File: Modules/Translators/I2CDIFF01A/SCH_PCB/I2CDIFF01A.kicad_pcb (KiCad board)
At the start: 2 copper layers, 40.1 x 50.3 mm, 55 parts, among them J1 JUMP_4X2, J10 JUMP_3X2, J11 JUMP2_2x1, J12 CONN_3, J13 JUMP_3X2, J14 JUMP2_2x1, J15 CONN_3, J16 EN, J17 JUMP2_2x1, J19 JUMP_2x1, J2 RJ45_RJHSE-5384, J20 JUMP_2x1, J21 JUMP_2x1, J22 JUMP_2x1, J23 JUMP_2x1, J3 JUMP_2x1, J4 JUMP_2x1, J5 JUMP_2x1, J6 JUMP_2x1, J7 JUMP_2x1, J8 JUMP_2x1, J9 JUMP_2x1, M1 HOLE, M2 HOLE, M3 HOLE, M4 HOLE, U1 LM1117 5V, U2 LM1117 3V3, U3 PCA9616

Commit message: vylepseni layoutu.
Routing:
- net /SCL-: track 41.5 -> 39.9 mm
- net /SCL+: track 40.7 -> 39.2 mm
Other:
- rule via_min_size: 0.89 -> 0.7

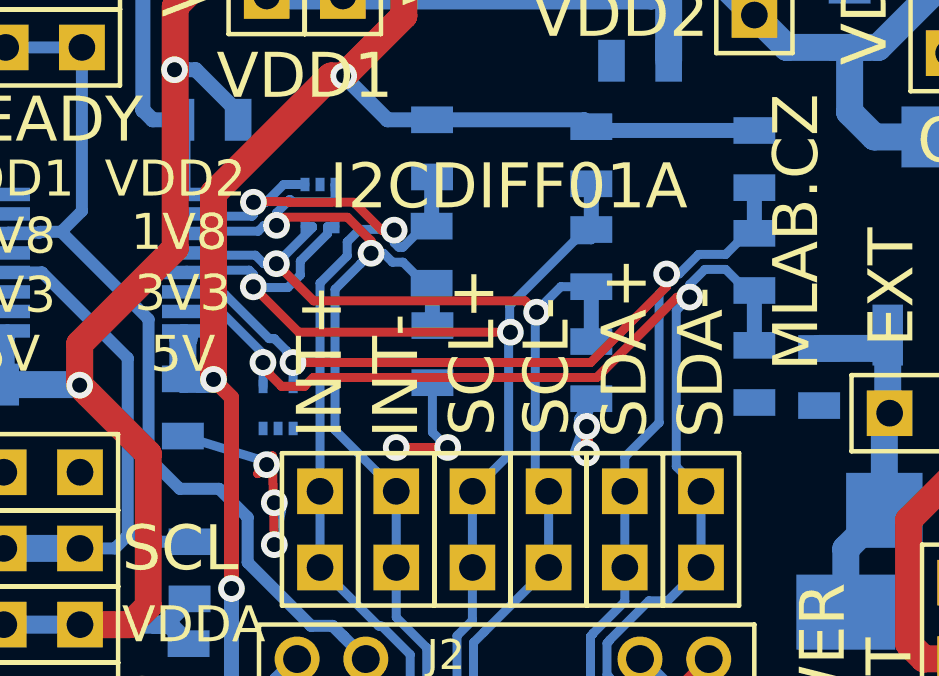
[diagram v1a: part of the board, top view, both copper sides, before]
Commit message: 
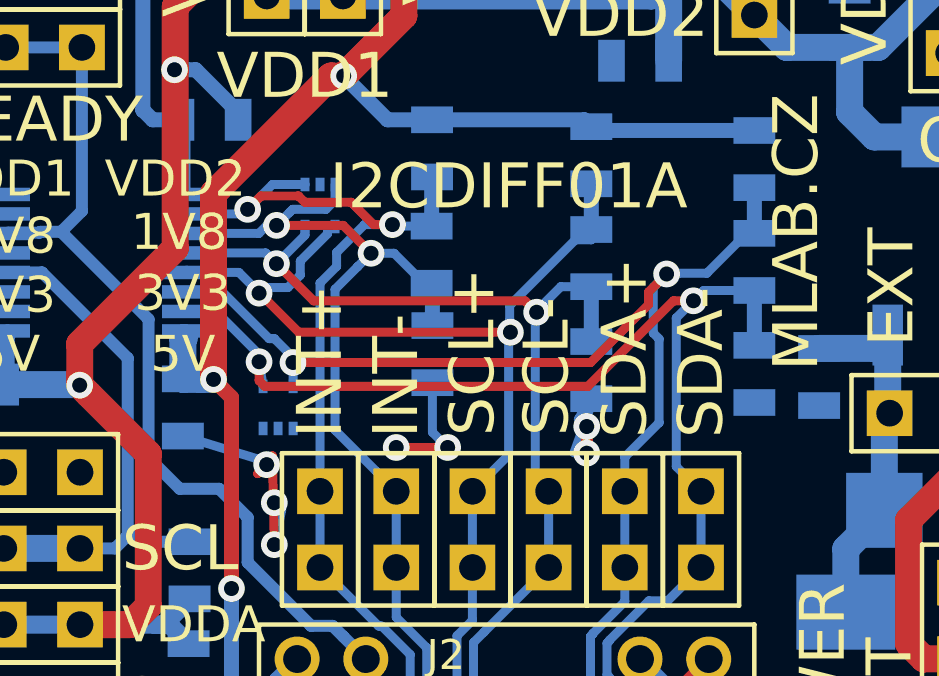
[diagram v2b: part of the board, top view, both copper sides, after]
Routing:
- net /INT-: track 37.3 -> 36.6 mm
- net /SDA-: track 46.3 -> 45.6 mm

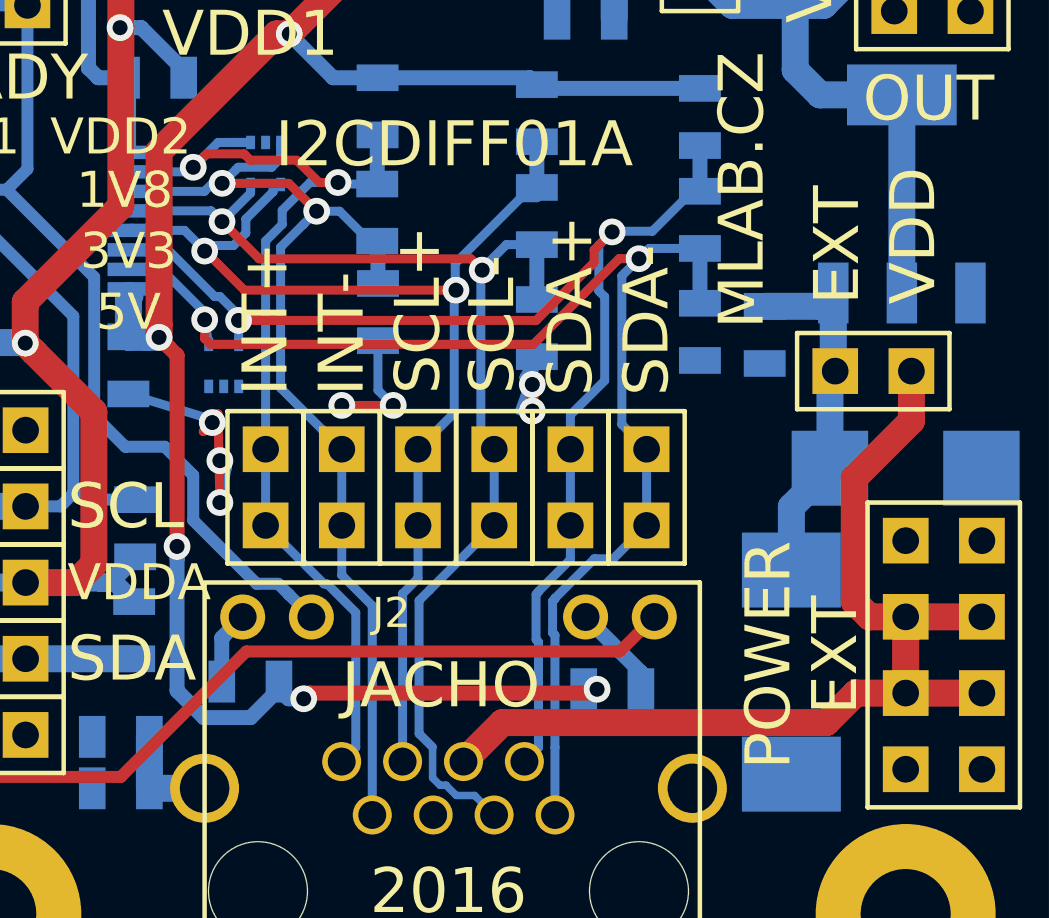
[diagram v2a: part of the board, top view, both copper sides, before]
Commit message: vylepseni layoutu differencnich cest.
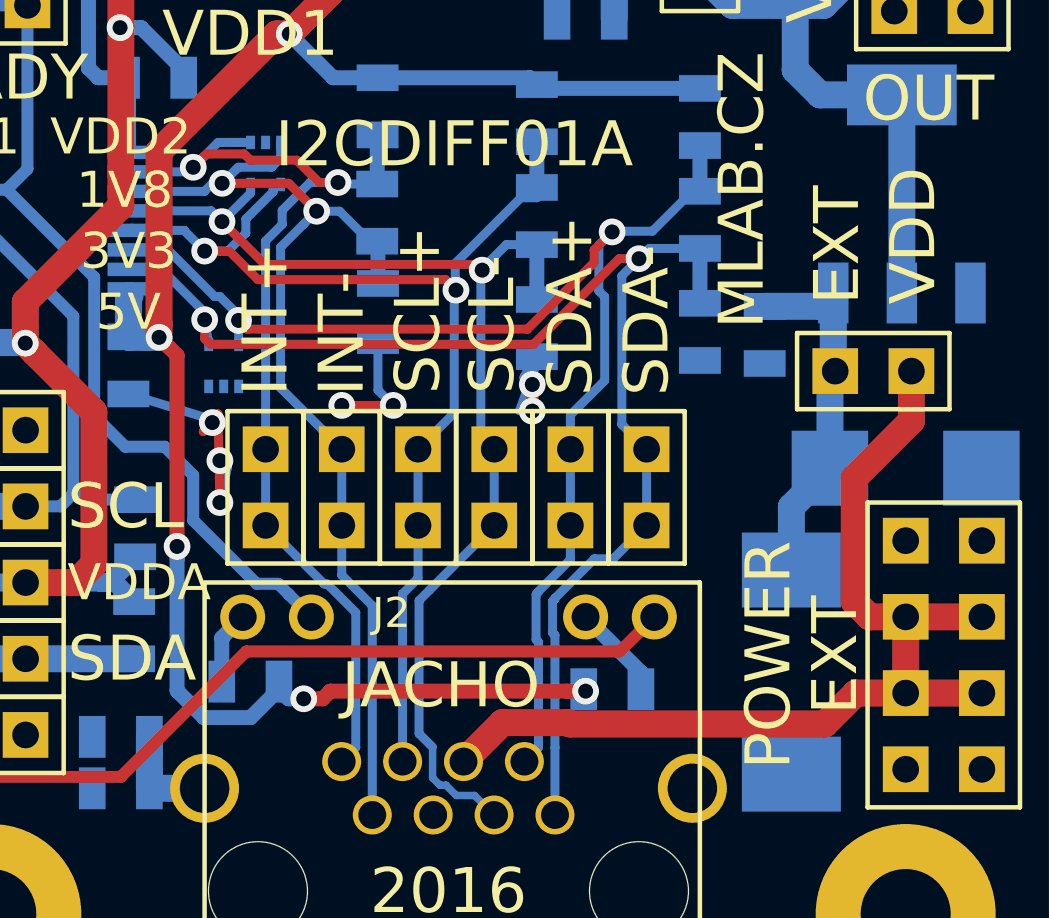
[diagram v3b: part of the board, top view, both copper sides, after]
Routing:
- net /VddB: track 65.4 -> 64.6 mm
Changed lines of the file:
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@@
-(kicad_pcb (version 4) (host pcbnew 4.0.1-stable)
+(kicad_pcb (version 4) (host pcbnew 0.201602161416+6560~42~ubuntu15.10.1-product)
   (general
     (links 132)
@@
     (thickness 1.6)
     (drawings 44)
-    (tracks 413)
+    (tracks 420)
     (zones 0)
     (modules 55)
@@
     (visible_elements 7FFFFF7F)
     (pcbplotparams
-      (layerselection 0x010e0_80000001)
+      (layerselection 0x010e0_ffffffff)
       (usegerberextensions false)
       (excludeedgelayer true)
@@
       (hpglpenspeed 20)
       (hpglpendiameter 15)
-      (hpglpenoverlay 2)
       (psnegative false)
       (psa4output false)
@@
   (gr_line (start 40.386 -0.254) (end 40.386 -50.546) (angle 90) (layer Edge.Cuts) (width 0.1))
   (gr_line (start 0.254 -0.254) (end 40.386 -0.254) (angle 90) (layer Edge.Cuts) (width 0.1))
+  (segment (start 24.318897 -11.462001) (end 24.366399 -11.414499) (width 0.9) (layer F.Cu) (net 1))
+  (segment (start 20.82 -10.162) (end 22.120001 -11.462001) (width 0.9) (layer F.Cu) (net 1))
+  (segment (start 22.120001 -11.462001) (end 24.318897 -11.462001) (width 0.9) (layer F.Cu) (net 1))
+  (segment (start 24.366399 -11.414499) (end 32.866499 -11.414499) (width 0.9) (layer F.Cu) (net 1))
+  (segment (start 32.866499 -11.414499) (end 33.898 -12.446) (width 0.9) (layer F.Cu) (net 1))
   (segment (start 33.898 -12.446) (end 35.56 -12.446) (width 0.9) (layer F.Cu) (net 1))
-  (segment (start 32.914001 -11.462001) (end 33.898 -12.446) (width 0.9) (layer F.Cu) (net 1))
-  (segment (start 22.120001 -11.462001) (end 32.914001 -11.462001) (width 0.9) (layer F.Cu) (net 1))
-  (segment (start 20.82 -10.162) (end 22.120001 -11.462001) (width 0.9) (layer F.Cu) (net 1))
   (segment (start 35.56 -12.446) (end 38.1 -12.446) (width 0.9) (layer F.Cu) (net 1))
   (segment (start 35.56 -12.446) (end 35.56 -14.986) (width 0.9) (layer F.Cu) (net 1))
@@
   (segment (start 23.368 -48.133) (end 23.368 -45.593) (width 0.9) (layer B.Cu) (net 4))
   (segment (start 12.446 -42.164) (end 14.986 -42.164) (width 0.9) (layer B.Cu) (net 4))
-  (segment (start 25.273 -12.573) (end 25.146 -12.446) (width 0.5) (layer F.Cu) (net 5))
-  (segment (start 15.6845 -12.446) (end 15.494 -12.2555) (width 0.5) (layer F.Cu) (net 5))
-  (segment (start 25.146 -12.446) (end 15.6845 -12.446) (width 0.5) (layer F.Cu) (net 5))
+  (segment (start 24.262675 -12.5095) (end 24.892 -12.5095) (width 0.5) (layer F.Cu) (net 5))
+  (segment (start 16.377325 -12.5095) (end 24.262675 -12.5095) (width 0.5) (layer F.Cu) (net 5))
+  (via (at 24.892 -12.5095) (size 0.89) (drill 0.5) (layers F.Cu B.Cu) (net 5))
+  (segment (start 16.123325 -12.2555) (end 16.377325 -12.5095) (width 0.5) (layer F.Cu) (net 5))
+  (segment (start 15.494 -12.2555) (end 16.123325 -12.2555) (width 0.5) (layer F.Cu) (net 5))
+  (segment (start 24.8285 -12.573) (end 24.892 -12.5095) (width 0.5) (layer B.Cu) (net 5))
   (segment (start 14.986 -12.2555) (end 15.069736 -12.2555) (width 0.5) (layer B.Cu) (net 5))
   (segment (start 14.6685 -12.573) (end 14.986 -12.2555) (width 0.5) (layer B.Cu) (net 5))
@@
   (segment (start 9.7064 -25.919) (end 9.7064 -24.3749) (width 0.25) (layer B.Cu) (net 5))
   (segment (start 9.7064 -24.3749) (end 9.652 -24.3205) (width 0.25) (layer B.Cu) (net 5))
-  (segment (start 24.8285 -12.573) (end 25.273 -12.573) (width 0.5) (layer B.Cu) (net 5))
-  (via (at 25.273 -12.573) (size 0.89) (drill 0.5) (layers F.Cu B.Cu) (net 5))
   (segment (start 28.702 -32.6009) (end 23.3934 -32.6009) (width 0.5) (layer B.Cu) (net 5))
   (segment (start 23.3934 -32.6009) (end 23.2664 -32.7279) (width 0.5) (layer B.Cu) (net 5))
@@
   (segment (start 17.78 -8.382) (end 17.78 -15.357806) (width 0.3) (layer B.Cu) (net 12))
   (segment (start 17.9578 -27.4955) (end 17.9451 -27.5082) (width 0.5) (layer B.Cu) (net 12))
-  (segment (start 21.443851 -26.542524) (end 21.066375 -26.92) (width 0.3) (layer F.Cu) (net 13))
-  (segment (start 21.066375 -26.92) (end 14.011074 -26.92) (width 0.3) (layer F.Cu) (net 13))
-  (segment (start 14.011074 -26.92) (end 12.770702 -28.160372) (width 0.3) (layer F.Cu) (net 13))
+  (segment (start 21.443851 -26.542524) (end 21.252875 -26.7335) (width 0.3) (layer F.Cu) (net 13))
+  (segment (start 21.252875 -26.7335) (end 14.197574 -26.7335) (width 0.3) (layer F.Cu) (net 13))
+  (segment (start 14.197574 -26.7335) (end 12.770702 -28.160372) (width 0.3) (layer F.Cu) (net 13))
   (segment (start 9.7064 -28.519) (end 12.412074 -28.519) (width 0.3) (layer B.Cu) (net 13))
   (segment (start 12.412074 -28.519) (end 12.770702 -28.160372) (width 0.3) (layer B.Cu) (net 13))
@@
   (segment (start 19.339999 -15.529999) (end 19.692908 -15.882908) (width 0.3) (layer B.Cu) (net 13))
   (segment (start 19.692908 -15.882908) (end 21.844 -18.034) (width 0.3) (layer B.Cu) (net 13))
+  (segment (start 11.520582 -27.869) (end 11.520582 -27.849418) (width 0.3) (layer B.Cu) (net 14))
+  (segment (start 11.520582 -27.849418) (end 12.192 -27.178) (width 0.3) (layer B.Cu) (net 14))
+  (segment (start 14.72438 -29.39796) (end 14.474 -29.39796) (width 0.3) (layer B.Cu) (net 14))
+  (segment (start 14.474 -29.39796) (end 14.474 -29.156564) (width 0.3) (layer B.Cu) (net 14))
+  (segment (start 14.474 -29.156564) (end 13.565703 -28.248267) (width 0.3) (layer B.Cu) (net 14))
+  (segment (start 13.565703 -28.248267) (end 13.565703 -27.778771) (width 0.3) (layer B.Cu) (net 14))
+  (segment (start 13.565703 -27.778771) (end 12.964932 -27.178) (width 0.3) (layer B.Cu) (net 14))
+  (segment (start 12.964932 -27.178) (end 12.192 -27.178) (width 0.3) (layer B.Cu) (net 14))
+  (via (at 12.192 -27.178) (size 0.89) (drill 0.5) (layers F.Cu B.Cu) (net 14))
+  (segment (start 20.569627 -25.875237) (end 20.219364 -26.2255) (width 0.3) (layer F.Cu) (net 14))
+  (segment (start 12.821325 -27.178) (end 12.192 -27.178) (width 0.3) (layer F.Cu) (net 14))
+  (segment (start 20.219364 -26.2255) (end 13.97 -26.2255) (width 0.3) (layer F.Cu) (net 14))
+  (segment (start 13.97 -26.2255) (end 13.023175 -27.172325) (width 0.3) (layer F.Cu) (net 14))
+  (segment (start 13.023175 -27.172325) (end 12.827 -27.172325) (width 0.3) (layer F.Cu) (net 14))
+  (segment (start 12.827 -27.172325) (end 12.821325 -27.178) (width 0.3) (layer F.Cu) (net 14))
   (segment (start 9.7064 -27.869) (end 11.520582 -27.869) (width 0.3) (layer B.Cu) (net 14))
-  (segment (start 11.520582 -27.869) (end 11.999956 -27.389626) (width 0.3) (layer B.Cu) (net 14))
-  (segment (start 20.569627 -25.875237) (end 13.514345 -25.875237) (width 0.3) (layer F.Cu) (net 14))
-  (segment (start 13.514345 -25.875237) (end 11.999956 -27.389626) (width 0.3) (layer F.Cu) (net 14))
   (segment (start 19.304 -20.574) (end 20.5105 -21.7805) (width 0.3) (layer B.Cu) (net 14))
   (segment (start 20.5105 -21.7805) (end 20.5105 -25.81611) (width 0.3) (layer B.Cu) (net 14))
@@
   (segment (start 22.733 -28.956) (end 23.2664 -28.956) (width 0.3) (layer B.Cu) (net 14))
   (segment (start 23.2664 -28.956) (end 23.2664 -29.2989) (width 0.3) (layer B.Cu) (net 14))
-  (segment (start 11.999956 -27.389626) (end 12.364846 -27.389626) (width 0.3) (layer B.Cu) (net 14))
-  (segment (start 12.364846 -27.389626) (end 12.389101 -27.365371) (width 0.3) (layer B.Cu) (net 14))
-  (segment (start 12.389101 -27.365371) (end 13.152303 -27.365371) (width 0.3) (layer B.Cu) (net 14))
-  (segment (start 14.474 -29.156564) (end 14.474 -29.39796) (width 0.3) (layer B.Cu) (net 14))
-  (segment (start 13.152303 -27.365371) (end 13.565703 -27.778771) (width 0.3) (layer B.Cu) (net 14))
-  (segment (start 14.474 -29.39796) (end 14.72438 -29.39796) (width 0.3) (layer B.Cu) (net 14))
-  (segment (start 13.565703 -27.778771) (end 13.565703 -28.248267) (width 0.3) (layer B.Cu) (net 14))
-  (segment (start 13.565703 -28.248267) (end 14.474 -29.156564) (width 0.3) (layer B.Cu) (net 14))
   (via (at 20.569627 -25.875237) (size 0.89) (drill 0.5) (layers F.Cu B.Cu) (net 14))
-  (via (at 12.192 -27.178) (size 0.89) (drill 0.5) (layers F.Cu B.Cu) (net 14))
   (segment (start 23.2664 -29.2989) (end 23.0124 -29.2989) (width 0.3) (layer B.Cu) (net 14))
   (segment (start 19.304 -18.034) (end 19.304 -20.574) (width 0.3) (layer B.Cu) (net 14))
@@
   (segment (start 9.7064 -27.869) (end 9.781399 -27.943999) (width 0.3) (layer B.Cu) (net 14))
   (segment (start 23.2664 -29.2989) (end 23.2664 -30.8229) (width 0.5) (layer B.Cu) (net 14))
-  (segment (start 23.243047 -24.8666) (end 25.17344 -26.797007) (width 0.3) (layer F.Cu) (net 15))
-  (segment (start 25.776627 -27.817373) (end 25.17344 -27.214186) (width 0.3) (layer F.Cu) (net 15))
-  (segment (start 25.17344 -27.214186) (end 25.17344 -26.797007) (width 0.3) (layer F.Cu) (net 15))
+  (segment (start 13.3223 -24.8666) (end 13.6144 -24.5745) (width 0.3) (layer F.Cu) (net 15))
+  (segment (start 13.6144 -24.5745) (end 22.950933 -24.5745) (width 0.3) (layer F.Cu) (net 15))
+  (segment (start 22.950933 -24.5745) (end 25.17344 -26.797007) (width 0.3) (layer F.Cu) (net 15))
+  (segment (start 25.17344 -26.797007) (end 25.17344 -27.214186) (width 0.3) (layer F.Cu) (net 15))
+  (segment (start 25.17344 -27.214186) (end 25.776627 -27.817373) (width 0.3) (layer F.Cu) (net 15))
   (segment (start 25.527 -22.86) (end 25.527 -25.654) (width 0.3) (layer B.Cu) (net 15))
   (segment (start 25.527 -25.654) (end 25.331628 -25.849372) (width 0.3) (layer B.Cu) (net 15))
@@
   (segment (start 24.384 -21.717) (end 25.527 -22.86) (width 0.3) (layer B.Cu) (net 15))
   (via (at 25.776627 -27.817373) (size 0.89) (drill 0.5) (layers F.Cu B.Cu) (net 15))
-  (segment (start 13.3223 -24.8666) (end 23.243047 -24.8666) (width 0.3) (layer F.Cu) (net 15))
   (via (at 13.3223 -24.8666) (size 0.89) (drill 0.5) (layers F.Cu B.Cu) (net 15))
   (segment (start 24.384 -18.034) (end 24.384 -16.898908) (width 0.3) (layer B.Cu) (net 15))

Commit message: 
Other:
- rule pad_to_mask_clearance: 0 -> 0.12
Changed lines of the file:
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@@
-(kicad_pcb (version 4) (host pcbnew 0.201602161416+6560~42~ubuntu15.10.1-product)
+(kicad_pcb (version 4) (host pcbnew 4.0.1-stable)
   (general
     (links 132)
@@
     (pad_size 1.5 1.5)
     (pad_drill 0.6)
-    (pad_to_mask_clearance 0)
+    (pad_to_mask_clearance 0.12)
     (aux_axis_origin 0 0)
     (visible_elements 7FFFFF7F)
     (pcbplotparams
-      (layerselection 0x010e0_ffffffff)
+      (layerselection 0x010e0_80000001)
       (usegerberextensions false)
       (excludeedgelayer true)
@@
       (hpglpenspeed 20)
       (hpglpendiameter 15)
+      (hpglpenoverlay 2)
       (psnegative false)
       (psa4output false)

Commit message: Nahrani dokumentace
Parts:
- C1: value 10uF -> 10uF/16V
- D1: value SM15T18A -> SMBJ15A-E3/52
- R11, R3, R5, R6, R8, R9: value 600 -> 620
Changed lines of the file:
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@@
     (links 132)
     (no_connects 0)
-    (area -4.6355 -53.467 44.577001 4.953001)
+    (area 0.203999 -50.596001 40.436001 -0.203999)
     (thickness 1.6)
     (drawings 44)
@@
       (effects (font (size 0.50038 0.50038) (thickness 0.10922)) (justify mirror))
     )
-    (fp_text value 10uF (at 0.127 -0.381 270) (layer B.SilkS)
+    (fp_text value 10uF/16V (at 0.127 -0.381 270) (layer B.SilkS)
       (effects (font (size 0.50038 0.50038) (thickness 0.10922)) (justify mirror))
     )
@@
       (effects (font (size 0.50038 0.50038) (thickness 0.10922)) (justify mirror))
     )
-    (fp_text value 600 (at 0.127 -0.381 270) (layer B.SilkS)
+    (fp_text value 620 (at 0.127 -0.381 270) (layer B.SilkS)
       (effects (font (size 0.50038 0.50038) (thickness 0.10922)) (justify mirror))
     )
@@
       (effects (font (size 0.50038 0.50038) (thickness 0.10922)) (justify mirror))
     )
-    (fp_text value 600 (at 0.127 -0.381 270) (layer B.SilkS)
+    (fp_text value 620 (at 0.127 -0.381 270) (layer B.SilkS)
       (effects (font (size 0.50038 0.50038) (thickness 0.10922)) (justify mirror))
     )
@@
       (effects (font (size 0.50038 0.50038) (thickness 0.10922)) (justify mirror))
     )
-    (fp_text value 600 (at 0.127 -0.381 270) (layer B.SilkS)
+    (fp_text value 620 (at 0.127 -0.381 270) (layer B.SilkS)
       (effects (font (size 0.50038 0.50038) (thickness 0.10922)) (justify mirror))
     )
@@
       (effects (font (size 0.50038 0.50038) (thickness 0.10922)) (justify mirror))
     )
-    (fp_text value 600 (at 0.127 -0.381 270) (layer B.SilkS)
+    (fp_text value 620 (at 0.127 -0.381 270) (layer B.SilkS)
       (effects (font (size 0.50038 0.50038) (thickness 0.10922)) (justify mirror))
     )
@@
       (effects (font (size 0.50038 0.50038) (thickness 0.10922)) (justify mirror))
     )
-    (fp_text value 600 (at 0.127 -0.381 270) (layer B.SilkS)
+    (fp_text value 620 (at 0.127 -0.381 270) (layer B.SilkS)
       (effects (font (size 0.50038 0.50038) (thickness 0.10922)) (justify mirror))
     )
@@
       (effects (font (size 0.50038 0.50038) (thickness 0.10922)) (justify mirror))
     )
-    (fp_text value 600 (at 0.127 -0.381 270) (layer B.SilkS)
+    (fp_text value 620 (at 0.127 -0.381 270) (layer B.SilkS)
       (effects (font (size 0.50038 0.50038) (thickness 0.10922)) (justify mirror))
     )
@@
       (effects (font (thickness 0.3048)) (justify mirror))
     )
-    (fp_text value SM15T18A (at 0 -5.08 90) (layer B.SilkS) hide
+    (fp_text value SMBJ15A-E3/52 (at 0 -5.08 90) (layer B.SilkS) hide
       (effects (font (thickness 0.3048)) (justify mirror))
     )
